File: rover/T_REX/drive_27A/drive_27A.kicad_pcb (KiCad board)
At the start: 4 copper layers, 32.5 x 59.3 mm, 53 parts, among them J1 USB_B_Micro, J2 RJ45, J6 XT60PW-M, J7 XT60PW-F, J9 B4B-XH-A_LF__SN_, SW1 TS09-63-25-WT-160-SMT-TR, SW2 TS09-63-25-WT-160-SMT-TR, U2 SN65HVD232Q, U3 LD1086DT33TR, U4 BTN8962TA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

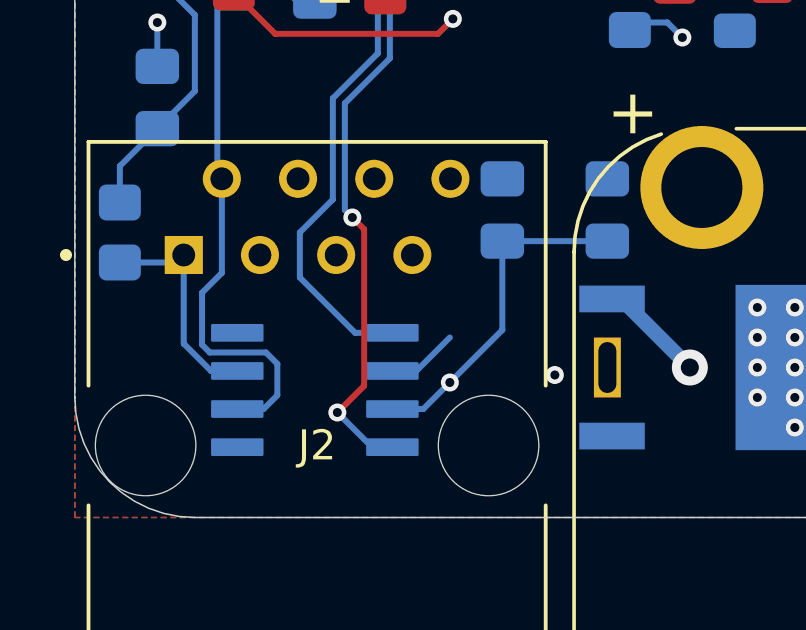
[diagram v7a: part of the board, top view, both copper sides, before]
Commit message: Now support 5v to 24v input from eth connector
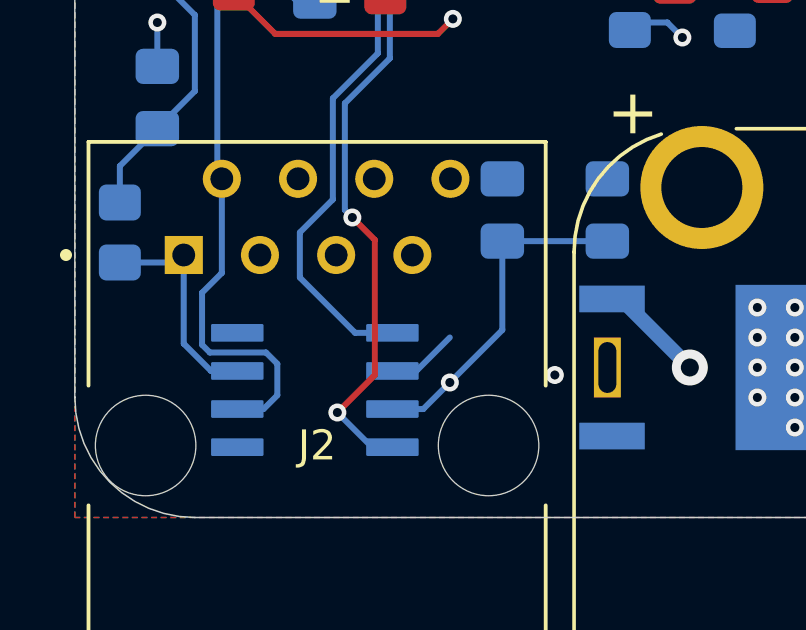
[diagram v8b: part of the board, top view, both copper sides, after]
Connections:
- J2 pad 7: +5V -> +24V_Logic
- JP1 pad 1: +24V -> +24V_Logic
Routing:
- net +5V: track 76.3 -> 21.3 mm
- net +24V_Logic: track 0.00 -> 47.4 mm
- net Net-(JP1-C): track 45.5 -> 45.0 mm
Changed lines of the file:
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@@
 	(net 66 "Net-(D3-Pad2)")
 	(net 67 "Net-(JP1-C)")
+	(net 68 "+24V_Logic")
 	(footprint "Connector_AMASS:AMASS_XT60PW-M_1x02_P7.20mm_Horizontal"
 		(layer "F.Cu")
@@
 			(layers "*.Cu" "*.Mask")
 			(remove_unused_layers no)
-			(net 4 "+5V")
+			(net 68 "+24V_Logic")
 			(pintype "passive")
 			(solder_mask_margin 0.102)
@@
 			(layers "*.Cu" "*.Mask")
 			(remove_unused_layers no)
-			(net 5 "+24V")
+			(net 68 "+24V_Logic")
 			(pinfunction "A")
 			(pintype "passive")
@@
 	)
 	(segment
-		(start 44.06 48.44)
-		(end 42.451667 50.048333)
-		(width 0.2)
-		(layer "In1.Cu")
-		(net 4)
-	)
-	(segment
-		(start 45 44.75)
-		(end 46.152537 45.902537)
-		(width 0.2)
-		(layer "In1.Cu")
-		(net 4)
-	)
-	(segment
-		(start 45.81 48.44)
-		(end 44.06 48.44)
-		(width 0.2)
-		(layer "In1.Cu")
-		(net 4)
-	)
-	(segment
-		(start 42.7 72.55)
-		(end 32.55 72.55)
-		(width 0.2)
-		(layer "In1.Cu")
-		(net 4)
-	)
-	(segment
 		(start 37.095 46.845)
 		(end 39.19 44.75)
@@
 	)
 	(segment
-		(start 44.05 71.2)
-		(end 42.7 72.55)
-		(width 0.2)
-		(layer "In1.Cu")
-		(net 4)
-	)
-	(segment
-		(start 44.227818 54.95)
-		(end 45.9 56.622182)
-		(width 0.2)
-		(layer "In1.Cu")
-		(net 4)
-	)
-	(segment
-		(start 42.95 54.95)
-		(end 44.227818 54.95)
-		(width 0.2)
-		(layer "In1.Cu")
-		(net 4)
-	)
-	(segment
-		(start 25.5 65.5)
-		(end 25.5 65)
-		(width 0.2)
-		(layer "In1.Cu")
-		(net 4)
-	)
-	(segment
-		(start 46.15274 48.09726)
-		(end 45.81 48.44)
-		(width 0.2)
-		(layer "In1.Cu")
-		(net 4)
-	)
-	(segment
-		(start 42.451667 54.451667)
-		(end 42.95 54.95)
-		(width 0.2)
-		(layer "In1.Cu")
-		(net 4)
-	)
-	(segment
-		(start 44.05 67.63684)
-		(end 44.05 71.2)
-		(width 0.2)
-		(layer "In1.Cu")
-		(net 4)
-	)
-	(segment
-		(start 42.451667 50.048333)
-		(end 42.451667 54.451667)
-		(width 0.2)
-		(layer "In1.Cu")
-		(net 4)
-	)
-	(segment
 		(start 39.19 44.75)
 		(end 45 44.75)
@@
 	)
 	(segment
-		(start 46.152537 45.902537)
-		(end 46.15274 48.09726)
-		(width 0.2)
-		(layer "In1.Cu")
-		(net 4)
-	)
-	(segment
-		(start 32.55 72.55)
-		(end 25.5 65.5)
-		(width 0.2)
-		(layer "In1.Cu")
-		(net 4)
-	)
-	(segment
-		(start 45.9 65.78684)
-		(end 44.05 67.63684)
-		(width 0.2)
-		(layer "In1.Cu")
-		(net 4)
-	)
-	(segment
-		(start 45.9 56.622182)
-		(end 45.9 65.78684)
-		(width 0.2)
-		(layer "In1.Cu")
-		(net 4)
-	)
-	(segment
 		(start 37.095 46.845)
 		(end 37.095 45)
@@
 	)
 	(segment
-		(start 23.5 63.75)
-		(end 23.894 64.144)
+		(start 24.25 69)
+		(end 23 70.25)
 		(width 0.2)
 		(layer "F.Cu")
@@
 	)
 	(segment
-		(start 23.894 69.356)
-		(end 23 70.25)
+		(start 23.5 63.75)
+		(end 24.25 64.5)
 		(width 0.2)
 		(layer "F.Cu")
@@
 	)
 	(segment
-		(start 23.894 64.144)
-		(end 23.894 69.356)
+		(start 24.25 64.5)
+		(end 24.25 69)
 		(width 0.2)
 		(layer "F.Cu")
@@
 	)
 	(segment
-		(start 43.797919 47.29)
-		(end 45 47.29)
+		(start 34.75 68.75)
+		(end 34.75 69.5)
 		(width 0.5)
 		(layer "In1.Cu")
@@
 	)
 	(segment
-		(start 35.5 70.25)
-		(end 37.25 72)
+		(start 41.75 54.25)
+		(end 41.75 51.75)
 		(width 0.5)
 		(layer "In1.Cu")
@@
 	)
 	(segment
-		(start 41.75 54.75)
-		(end 41.75 49.337919)
+		(start 45 65.25)
+		(end 45 56.5)
 		(width 0.5)
 		(layer "In1.Cu")
@@
 	)
 	(segment
-		(start 42.222182 72)
-		(end 43.5 70.722182)
+		(start 43.5 70.722182)
+		(end 43.5 66.75)
 		(width 0.5)
 		(layer "In1.Cu")
@@
 	)
 	(segment
-		(start 43.5 66.75)
-		(end 45 65.25)
+		(start 37.25 72)
+		(end 42.222182 72)
 		(width 0.5)
 		(layer "In1.Cu")
@@
 	)
 	(segment
-		(start 44 55.5)
-		(end 42.5 55.5)
+		(start 43.25 48.75)
+		(end 44.71 47.29)
 		(width 0.5)
 		(layer "In1.Cu")
@@
 	)
 	(segment
-		(start 35.5 68.75)
-		(end 35.5 70.25)
+		(start 34.75 69.5)
+		(end 37.25 72)
 		(width 0.5)
 		(layer "In1.Cu")
@@
 	)
 	(segment
-		(start 41.75 49.337919)
-		(end 43.797919 47.29)
+		(start 43 55.5)
+		(end 41.75 54.25)
 		(width 0.5)
 		(layer "In1.Cu")
@@
 	)
 	(segment
-		(start 45 65.25)
-		(end 45 56.5)
+		(start 44 55.5)
+		(end 43 55.5)
 		(width 0.5)
 		(layer "In1.Cu")
@@
 	)
 	(segment
-		(start 37.25 72)
-		(end 42.222182 72)
+		(start 43.5 66.75)
+		(end 45 65.25)
 		(width 0.5)
 		(layer "In1.Cu")
@@
 	)
 	(segment
-		(start 43.5 70.722182)
-		(end 43.5 66.75)
+		(start 42.222182 72)
+		(end 43.5 70.722182)
 		(width 0.5)
 		(layer "In1.Cu")
@@
 	)
 	(segment
-		(start 42.5 55.5)
-		(end 41.75 54.75)
+		(start 41.75 51.75)
+		(end 43.25 50.25)
 		(width 0.5)
 		(layer "In1.Cu")
@@
 	)
 	(segment
+		(start 43.25 50.25)
+		(end 43.25 48.75)
+		(width 0.5)
+		(layer "In1.Cu")
+		(net 67)
+	)
+	(segment
+		(start 44.71 47.29)
+		(end 45 47.29)
+		(width 0.5)
+		(layer "In1.Cu")
+		(net 67)
+	)
+	(segment
 		(start 43.5 66.75)
 		(end 43.5 66.9625)
@@
 		(net 67)
 	)
+	(segment
+		(start 42.75 54.25)
+		(end 43.45 54.95)
+		(width 0.2)
+		(layer "In1.Cu")
+		(net 68)
+	)
+	(segment
+		(start 44.05 71.2)
+		(end 42.7 72.55)
+		(width 0.2)
+		(layer "In1.Cu")
+		(net 68)
+	)
+	(segment
+		(start 45 49.83)
+		(end 42.75 52.08)
+		(width 0.2)
+		(layer "In1.Cu")
+		(net 68)
+	)
+	(segment
+		(start 45.9 65.78684)
+		(end 44.05 67.63684)
+		(width 0.2)
+		(layer "In1.Cu")
+		(net 68)
+	)
+	(segment
+		(start 42.75 52.08)
+		(end 42.75 54.25)
+		(width 0.2)
+		(layer "In1.Cu")
+		(net 68)
+	)
+	(segment
+		(start 45.9 56.622182)
+		(end 45.9 65.78684)
+		(width 0.2)
+		(layer "In1.Cu")
+		(net 68)
+	)
+	(segment
+		(start 32.55 72.55)
+		(end 25.5 65.5)
+		(width 0.2)
+		(layer "In1.Cu")
+		(net 68)
+	)
+	(segment
+		(start 43.45 54.95)
+		(end 44.227818 54.95)
+		(width 0.2)
+		(layer "In1.Cu")
+		(net 68)
+	)
+	(segment
+		(start 44.05 67.63684)
+		(end 44.05 71.2)
+		(width 0.2)
+		(layer "In1.Cu")
+		(net 68)
+	)
+	(segment
+		(start 42.7 72.55)
+		(end 32.55 72.55)
+		(width 0.2)
+		(layer "In1.Cu")
+		(net 68)
+	)
+	(segment
+		(start 44.227818 54.95)
+		(end 45.9 56.622182)
+		(width 0.2)
+		(layer "In1.Cu")
+		(net 68)
+	)
+	(segment
+		(start 25.5 65.5)
+		(end 25.5 65)
+		(width 0.2)
+		(layer "In1.Cu")
+		(net 68)
+	)
 	(zone
